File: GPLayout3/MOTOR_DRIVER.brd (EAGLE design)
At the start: 129.5 x 96.6 mm, 95 parts, among them T1 2N2222, T2 2N2222, U7 ATMEGA328P_TQFP, Y1 16MHz

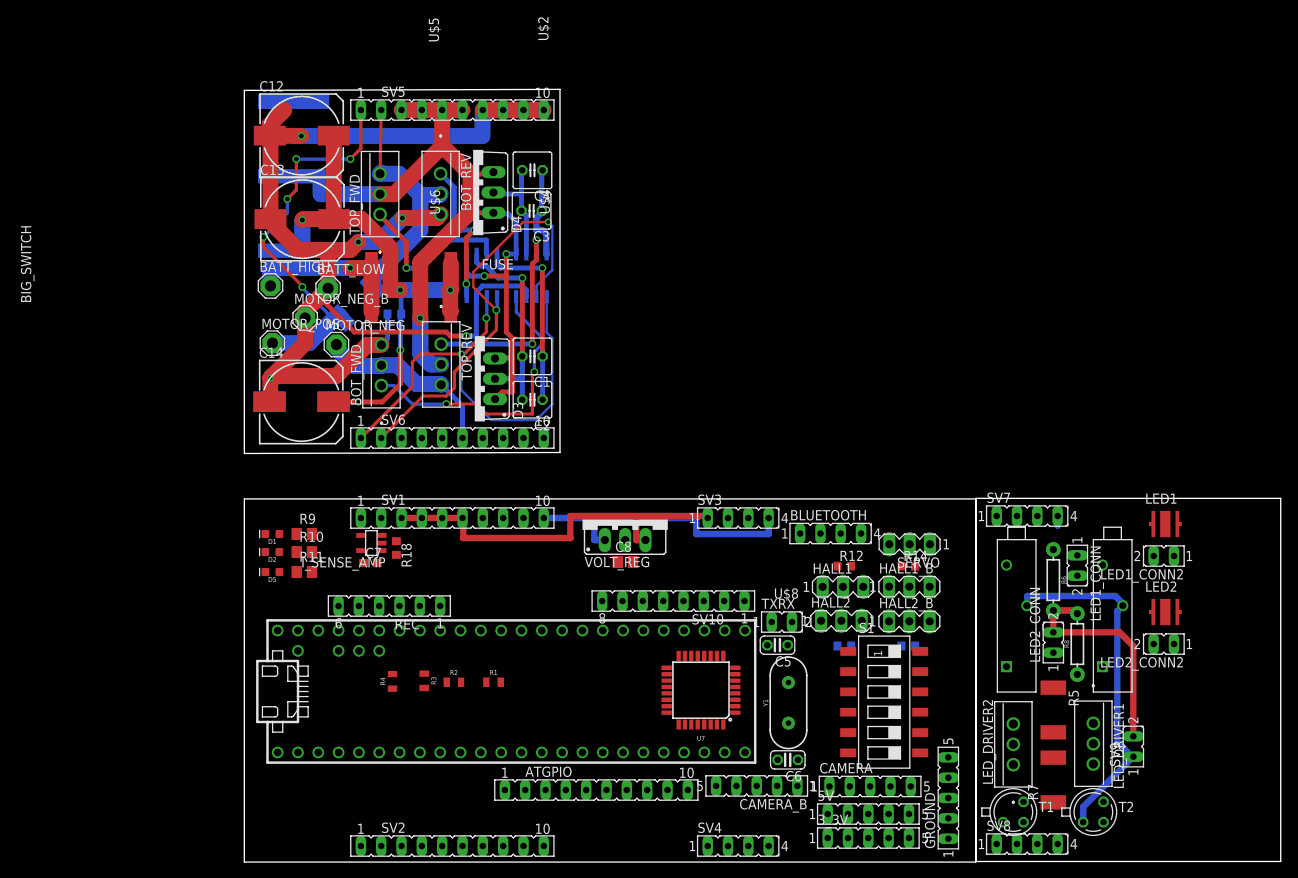
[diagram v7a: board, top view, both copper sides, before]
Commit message: Fixed errors on top board and moved current sense amp to top
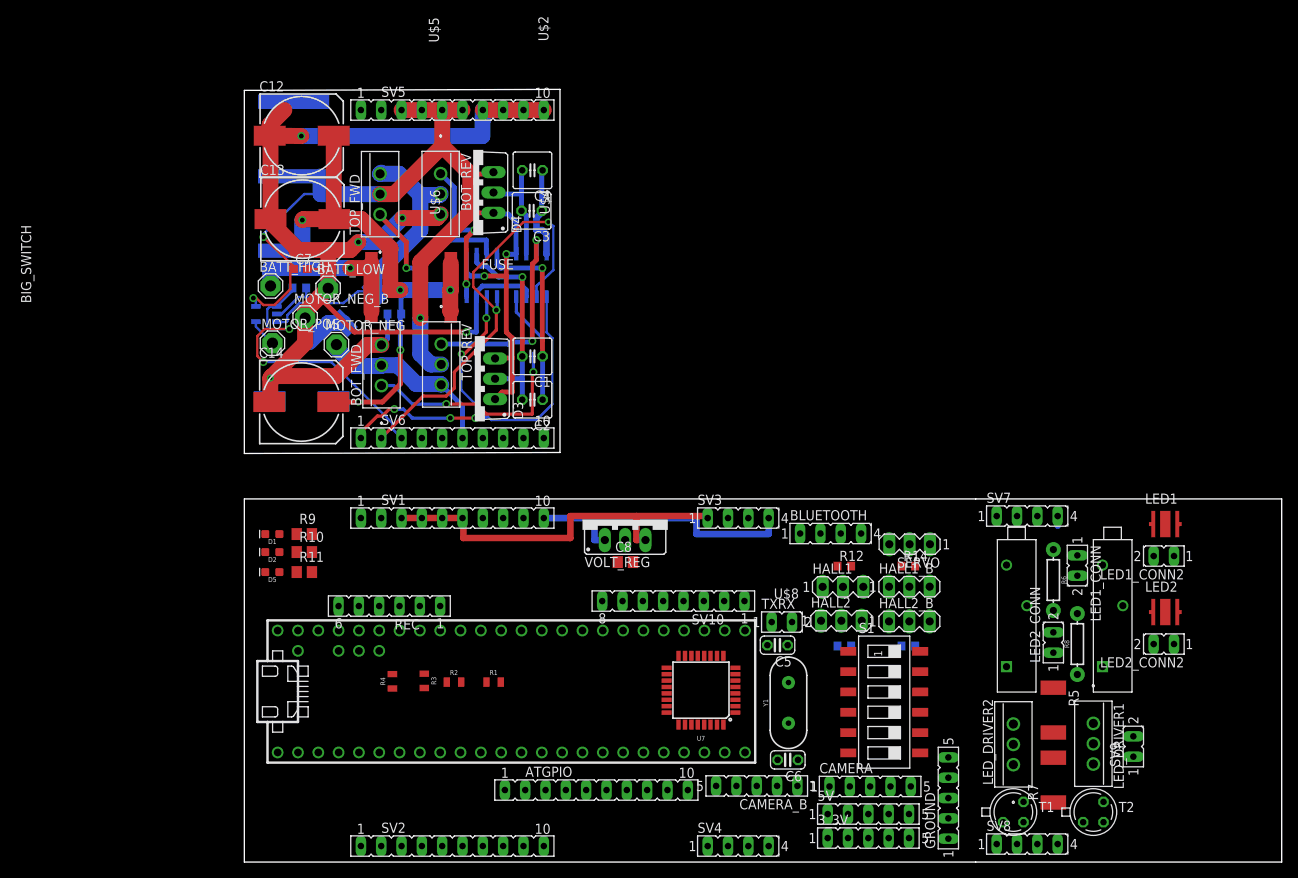
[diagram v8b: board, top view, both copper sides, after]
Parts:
- moved C7 37.8 mm to (7.00, 74.1)
- moved R18 34.7 mm to (6.88, 71.8), flipped to the bottom, turned to 0 degrees
- moved I_SENSE_AMP 31.5 mm to (2.75, 68.5), flipped to the bottom, turned to 270 degrees
- moved R17 0.67 mm to (14.4, 69.4)
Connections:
- new net I_SENSE_TOP: I_SENSE_AMP.1, R18.2, SV6.3
- net 7_4V: no longer C7.1, I_SENSE_AMP.5
- net 7_4V_TOP: now also C7.1, I_SENSE_AMP.5
- net GND: no longer C7.2, I_SENSE_AMP.2, R18.1
- net GND_TOP: now also C7.2, I_SENSE_AMP.2, R18.1
- net I_SENSE: no longer I_SENSE_AMP.1, R18.2
- net I_SENSE_HI: no longer I_SENSE_AMP.3
- net I_SENSE_HI_TOP: now also I_SENSE_AMP.3; no longer SV5.2
- net I_SENSE_LOW: no longer I_SENSE_AMP.4
- net I_SENSE_LOW_TOP: now also I_SENSE_AMP.4; no longer SV5.1
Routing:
- net GND_TOP2: track 45.9 -> 1.21 mm
- net I_SENSE_LOW_TOP: track 49.3 -> 9.02 mm, vias 5 -> 0
- net I_SENSE_TOP: track 0.00 -> 39.2 mm, vias 0 -> 2
- net 7_4V_TOP2: track 27.9 -> 0.00 mm
- net 7_4V_TOP: track 113.1 -> 138.0 mm, vias 3 -> 5
- net GND_TOP: track 159.5 -> 170.5 mm
- net I_SENSE_HI_TOP: track 30.7 -> 37.7 mm
- net N$9: track 36.9 -> 35.4 mm
- net LI_TOP: track 59.4 -> 59.0 mm, vias 2 -> 5
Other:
- board size 129.5 x 96.6 mm -> 129.7 x 96.6 mm
